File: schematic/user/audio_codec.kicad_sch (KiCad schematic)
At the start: 31 parts, among them U4 TLV320AIC3254IRHBR

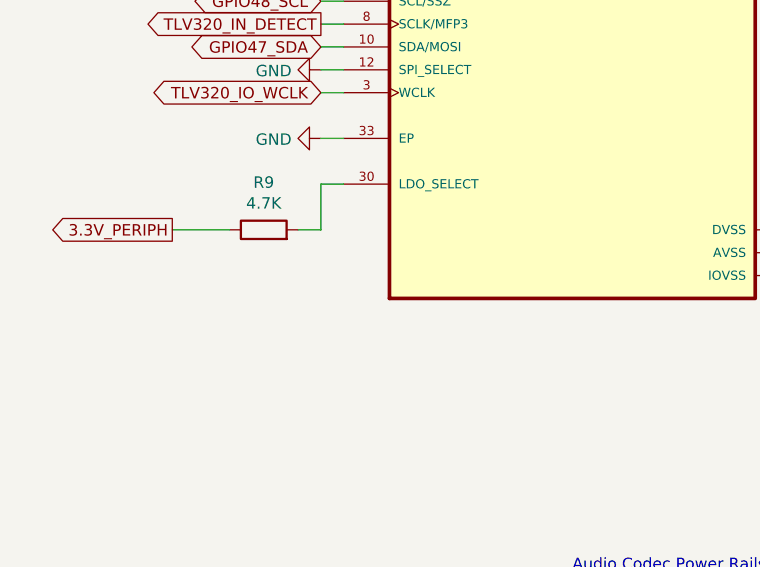
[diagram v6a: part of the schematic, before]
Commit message: v0.7 board: optimize component selection for USB input filter.
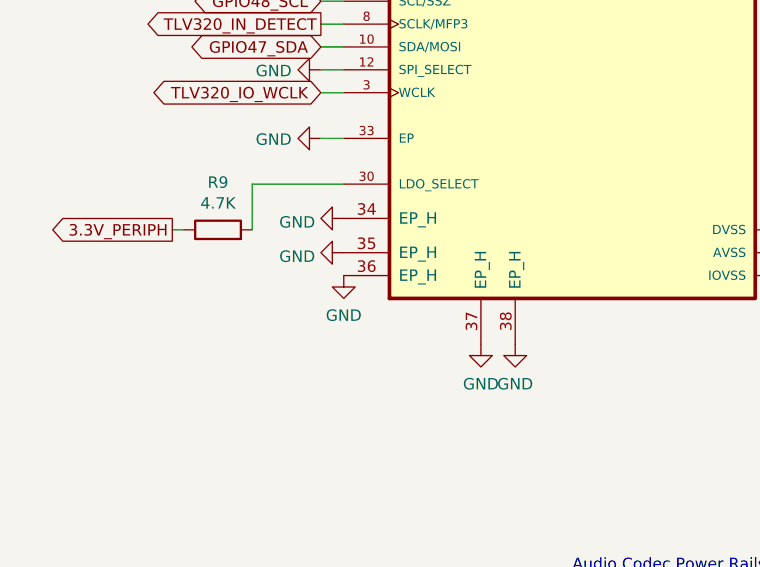
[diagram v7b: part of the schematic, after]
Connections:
- net GND: now also U4.34 (EP_H), U4.35 (EP_H), U4.36 (EP_H), U4.37 (EP_H), U4.38 (EP_H)
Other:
- moved on the sheet: R9
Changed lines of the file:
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@@
+    (stroke (width 0) (type default) (color 0 0 0 0))
+  )
+  (wire (pts (xy 34.29 124.46) (xy 35.56 124.46))
     (stroke (width 0) (type default) (color 0 0 0 0))
   )
@@
     (stroke (width 0) (type default) (color 0 0 0 0))
   )
-  (wire (pts (xy 40.64 124.46) (xy 34.29 124.46))
-    (stroke (width 0) (type default) (color 0 0 0 0))
-  )
   (wire (pts (xy 104.14 58.42) (xy 106.68 58.42))
     (stroke (width 0) (type default) (color 0 0 0 0))
@@
     (stroke (width 0) (type default) (color 0 0 0 0))
   )
+  (wire (pts (xy 43.18 119.38) (xy 53.34 119.38))
+    (stroke (width 0) (type default) (color 0 0 0 0))
+  )
   (wire (pts (xy 261.62 140.97) (xy 259.08 140.97))
     (stroke (width 0) (type default) (color 0 0 0 0))
@@
     (stroke (width 0) (type default) (color 0 0 0 0))
   )
-  (wire (pts (xy 53.34 119.38) (xy 50.8 119.38))
-    (stroke (width 0) (type default) (color 0 0 0 0))
-  )
   (wire (pts (xy 91.44 184.15) (xy 81.28 184.15))
     (stroke (width 0) (type default) (color 0 0 0 0))
@@
     (stroke (width 0) (type default) (color 0 0 0 0))
   )
-  (wire (pts (xy 48.26 124.46) (xy 50.8 124.46))
-    (stroke (width 0) (type default) (color 0 0 0 0))
-  )
   (wire (pts (xy 53.34 81.28) (xy 50.8 81.28))
     (stroke (width 0) (type default) (color 0 0 0 0))
@@
     (stroke (width 0) (type default) (color 0 0 0 0))
   )
+  (wire (pts (xy 43.18 124.46) (xy 43.18 119.38))
+    (stroke (width 0) (type default) (color 0 0 0 0))
+  )
   (wire (pts (xy 49.53 88.9) (xy 49.53 90.17))
     (stroke (width 0) (type default) (color 0 0 0 0))
@@
   )
   (wire (pts (xy 91.44 184.15) (xy 91.44 181.61))
-    (stroke (width 0) (type default) (color 0 0 0 0))
-  )
-  (wire (pts (xy 50.8 124.46) (xy 50.8 119.38))
     (stroke (width 0) (type default) (color 0 0 0 0))
   )
@@
     (pin "1")
     (pin "2")
+  )
+  (symbol (lib_id "power:GND") (at 53.34 127 270) (unit 1)
+    (in_bom yes) (on_board yes) (fields_autoplaced)
+    (property "Reference" "#PWR0112" (id 0) (at 46.99 127 0)
+      (effects (font (size 1.27 1.27)) hide)
+    )
+    (property "Value" "GND" (id 1) (at 50.1651 127.4338 90)
+      (effects (font (size 1.27 1.27)) (justify right))
+    )
+    (property "Footprint" "" (id 2) (at 53.34 127 0)
+      (effects (font (size 1.27 1.27)) hide)
+    )
+    (property "Datasheet" "" (id 3) (at 53.34 127 0)
+      (effects (font (size 1.27 1.27)) hide)
+    )
+    (pin "1")
   )
   (symbol (lib_id "Device:R") (at 149.86 52.07 0) (unit 1)
@@
     (pin "8")
     (pin "9")
+    (pin "36")
+    (pin "35")
+    (pin "34")
+    (pin "38")
+    (pin "37")
   )
   (symbol (lib_id "power:GND") (at 20.32 90.17 0) (unit 1)
@@
     (pin "1")
   )
+  (symbol (lib_id "power:GND") (at 68.58 137.16 0) (unit 1)
+    (in_bom yes) (on_board yes) (fields_autoplaced)
+    (property "Reference" "#PWR0113" (id 0) (at 68.58 143.51 0)
+      (effects (font (size 1.27 1.27)) hide)
+    )
+    (property "Value" "GND" (id 1) (at 68.58 141.6034 0))
+    (property "Footprint" "" (id 2) (at 68.58 137.16 0)
+      (effects (font (size 1.27 1.27)) hide)
+    )
+    (property "Datasheet" "" (id 3) (at 68.58 137.16 0)
+      (effects (font (size 1.27 1.27)) hide)
+    )
+    (pin "1")
+  )
   (symbol (lib_id "Device:R") (at 255.27 114.3 270) (unit 1)
     (in_bom yes) (on_board yes)
@@
     (pin "2")
   )
-  (symbol (lib_id "Device:R") (at 44.45 124.46 90) (unit 1)
-    (in_bom yes) (on_board yes)
-    (property "Reference" "R9" (id 0) (at 44.45 119.2022 90))
-    (property "Value" "4.7K" (id 1) (at 44.45 121.5136 90))
-    (property "Footprint" "Resistor_SMD:R_0402_1005Metric" (id 2) (at 44.45 126.238 90)
-      (effects (font (size 1.27 1.27)) hide)
-    )
-    (property "Datasheet" "https://datasheet.lcsc.com/lcsc/2110260030_UNI-ROYAL-Uniroyal-Elec-0402WGF4701TCE_C25900.pdf" (id 3) (at 44.45 124.46 0)
-      (effects (font (size 1.27 1.27)) hide)
-    )
-    (property "LCSC" "C25900" (id 4) (at 44.45 124.46 0)
+  (symbol (lib_id "Device:R") (at 39.37 124.46 90) (unit 1)
+    (in_bom yes) (on_board yes)
+    (property "Reference" "R9" (id 0) (at 39.37 119.2022 90))
+    (property "Value" "4.7K" (id 1) (at 39.37 121.5136 90))
+    (property "Footprint" "Resistor_SMD:R_0402_1005Metric" (id 2) (at 39.37 126.238 90)
+      (effects (font (size 1.27 1.27)) hide)
+    )
+    (property "Datasheet" "https://datasheet.lcsc.com/lcsc/2110260030_UNI-ROYAL-Uniroyal-Elec-0402WGF4701TCE_C25900.pdf" (id 3) (at 39.37 124.46 0)
+      (effects (font (size 1.27 1.27)) hide)
+    )
+    (property "LCSC" "C25900" (id 4) (at 39.37 124.46 0)
       (effects (font (size 1.27 1.27)) hide)
     )
@@
     (pin "2")
   )
+  (symbol (lib_id "power:GND") (at 53.34 129.54 0) (unit 1)
+    (in_bom yes) (on_board yes) (fields_autoplaced)
+    (property "Reference" "#PWR0115" (id 0) (at 53.34 135.89 0)
+      (effects (font (size 1.27 1.27)) hide)
+    )
+    (property "Value" "GND" (id 1) (at 53.34 133.9834 0))
+    (property "Footprint" "" (id 2) (at 53.34 129.54 0)
+      (effects (font (size 1.27 1.27)) hide)
+    )
+    (property "Datasheet" "" (id 3) (at 53.34 129.54 0)
+      (effects (font (size 1.27 1.27)) hide)
+    )
+    (pin "1")
+  )
+  (symbol (lib_id "power:GND") (at 53.34 123.19 270) (unit 1)
+    (in_bom yes) (on_board yes) (fields_autoplaced)
+    (property "Reference" "#PWR0116" (id 0) (at 46.99 123.19 0)
+      (effects (font (size 1.27 1.27)) hide)
+    )
+    (property "Value" "GND" (id 1) (at 50.1651 123.6238 90)
+      (effects (font (size 1.27 1.27)) (justify right))
+    )
+    (property "Footprint" "" (id 2) (at 53.34 123.19 0)
+      (effects (font (size 1.27 1.27)) hide)
+    )
+    (property "Datasheet" "" (id 3) (at 53.34 123.19 0)
+      (effects (font (size 1.27 1.27)) hide)
+    )
+    (pin "1")
+  )
   (symbol (lib_id "Device:R") (at 248.92 27.94 270) (unit 1)
     (in_bom yes) (on_board yes)
@@
     (pin "2")
   )
+  (symbol (lib_id "power:GND") (at 72.39 137.16 0) (unit 1)
+    (in_bom yes) (on_board yes) (fields_autoplaced)
+    (property "Reference" "#PWR0114" (id 0) (at 72.39 143.51 0)
+      (effects (font (size 1.27 1.27)) hide)
+    )
+    (property "Value" "GND" (id 1) (at 72.39 141.6034 0))
+    (property "Footprint" "" (id 2) (at 72.39 137.16 0)
+      (effects (font (size 1.27 1.27)) hide)
+    )
+    (property "Datasheet" "" (id 3) (at 72.39 137.16 0)
+      (effects (font (size 1.27 1.27)) hide)
+    )
+    (pin "1")
+  )
 )
